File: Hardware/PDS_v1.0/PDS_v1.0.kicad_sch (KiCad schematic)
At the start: 28 parts, among them J1 Conn_01x02, J10 Conn_01x02, J11 Conn_01x02, J12 Conn_01x02, J13 Conn_01x04, J14 Conn_01x04, J15 Conn_01x03, J2 Conn_01x02, J3 Conn_01x02, J4 Conn_01x02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

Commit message: PDS done
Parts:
- added H1, H2, H3, H4: MountingHole, MountingHole:MountingHole_3.2mm_M3, symbol Mechanical:MountingHole
- added J6: Conn_01x02, Connector_Molex:Molex_KK-254_AE-6410-02A_1x02_P2.54mm_Vertical, symbol Connector_Generic:Conn_01x02
- J10: renamed from J8; footprint Connector_Molex:Molex_KK-254_AE-6410-03A_1x03_P2.54mm_Vertical -> Connector_Molex:Molex_KK-254_AE-6410-02A_1x02_P2.54mm_Vertical
- J11: renamed from J5; footprint Connector_Molex:Molex_KK-254_AE-6410-03A_1x03_P2.54mm_Vertical -> Connector_Molex:Molex_KK-254_AE-6410-02A_1x02_P2.54mm_Vertical
- J12: renamed from J6; footprint Connector_Molex:Molex_KK-254_AE-6410-03A_1x03_P2.54mm_Vertical -> Connector_Molex:Molex_KK-254_AE-6410-02A_1x02_P2.54mm_Vertical
- J13: renamed from J7; footprint Connector_Molex:Molex_KK-254_AE-6410-03A_1x03_P2.54mm_Vertical -> Connector_Molex:Molex_KK-254_AE-6410-02A_1x02_P2.54mm_Vertical
- J14: renamed from J10; footprint Connector_Molex:Molex_KK-254_AE-6410-03A_1x03_P2.54mm_Vertical -> Connector_Molex:Molex_KK-254_AE-6410-02A_1x02_P2.54mm_Vertical
- J15: renamed from J11; footprint Connector_Molex:Molex_KK-254_AE-6410-03A_1x03_P2.54mm_Vertical -> Connector_Molex:Molex_KK-254_AE-6410-02A_1x02_P2.54mm_Vertical
- J16: renamed from J12; footprint Connector_Molex:Molex_KK-254_AE-6410-03A_1x03_P2.54mm_Vertical -> Connector_Molex:Molex_KK-254_AE-6410-02A_1x02_P2.54mm_Vertical
- J3: renamed from J1; footprint Connector_Molex:Molex_KK-254_AE-6410-03A_1x03_P2.54mm_Vertical -> Connector_Molex:Molex_KK-254_AE-6410-02A_1x02_P2.54mm_Vertical
- J4: footprint Connector_Molex:Molex_KK-254_AE-6410-03A_1x03_P2.54mm_Vertical -> Connector_Molex:Molex_KK-254_AE-6410-02A_1x02_P2.54mm_Vertical
- J5: renamed from J9; footprint Connector_Molex:Molex_KK-254_AE-6410-03A_1x03_P2.54mm_Vertical -> Connector_Molex:Molex_KK-254_AE-6410-02A_1x02_P2.54mm_Vertical
- J8: renamed from J2; footprint Connector_Molex:Molex_KK-254_AE-6410-03A_1x03_P2.54mm_Vertical -> Connector_Molex:Molex_KK-254_AE-6410-02A_1x02_P2.54mm_Vertical
- J9: renamed from J3; footprint Connector_Molex:Molex_KK-254_AE-6410-03A_1x03_P2.54mm_Vertical -> Connector_Molex:Molex_KK-254_AE-6410-02A_1x02_P2.54mm_Vertical
- renumbered J13 to J1, J14 to J2, J15 to J7
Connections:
- net +5V: now also J11.2 (Pin_2), J12.2 (Pin_2), J13.2 (Pin_2), J4.1 (Pin_1), TP2.1
- net +3V3: now reaches J10.2 (Pin_2), J3.1 (Pin_1), J8.2 (Pin_2), J9.2 (Pin_2), TP1.1
- net +12V: now reaches J14.2 (Pin_2), J15.2 (Pin_2), J16.2 (Pin_2), J5.1 (Pin_1), TP3.1
- net at U1.10 (XIN): now also J6.1 (Pin_1)
- net at U1.11 (XOUT): now also J6.2 (Pin_2)
- no-connect marks 2 -> 0

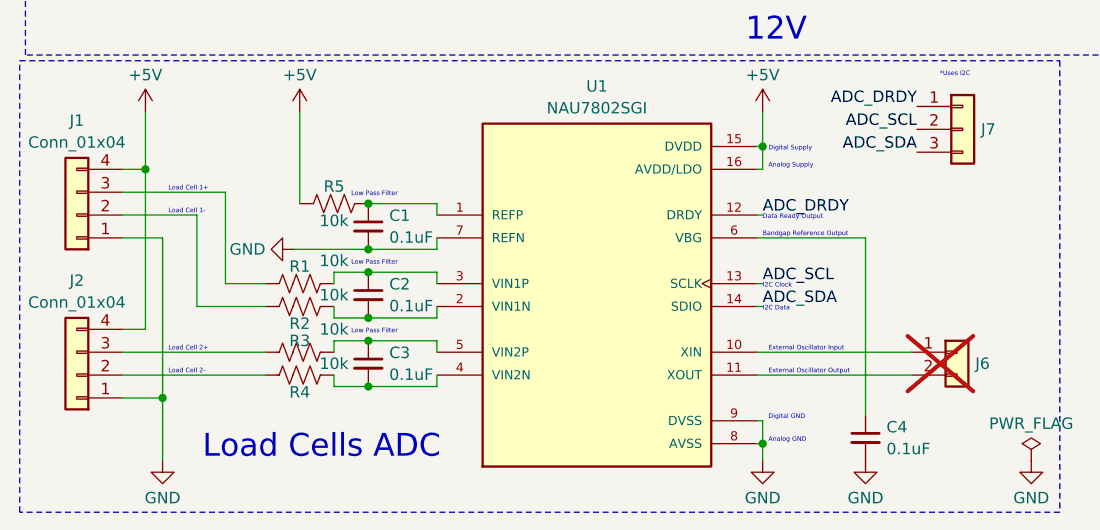
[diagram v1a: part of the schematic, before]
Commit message: fixed silkscreens + readability on PDS
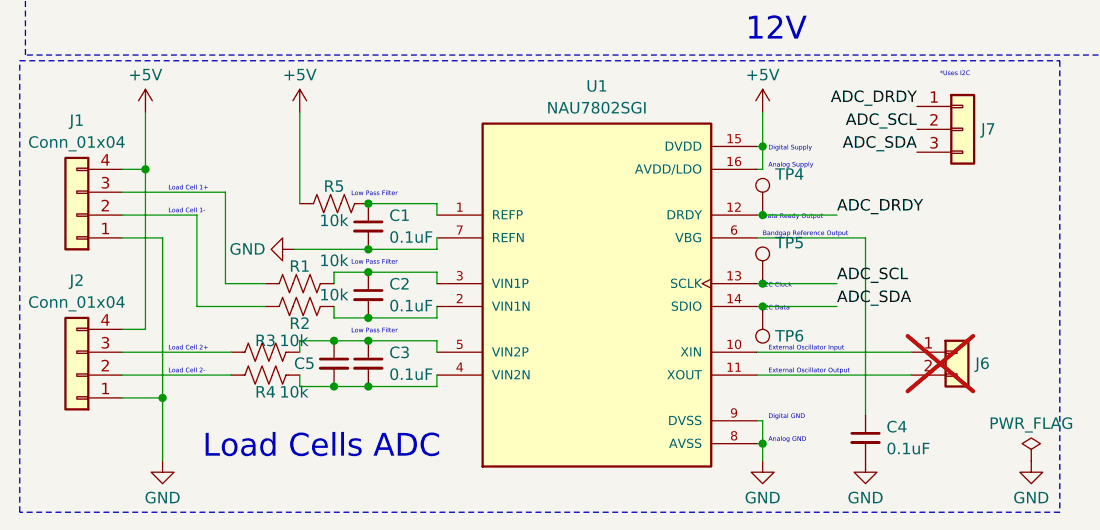
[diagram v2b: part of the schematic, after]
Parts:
- added C5: 470uF, Capacitor_THT:C_Radial_D10.0mm_H12.5mm_P5.00mm, symbol device:C_Small
- added TP4, TP5, TP6: TestPoint, TestPoint:TestPoint_Keystone_5010-5014_Multipurpose, symbol Connector:TestPoint
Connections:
- net ADC_DRDY: now also TP4.1
- net ADC_SCL: now also TP5.1
- net ADC_SDA: now also TP6.1
- net at C3.2, R4.2, U1.4 (VIN2N): now also C5.2
- net at C3.1, R3.2, U1.5 (VIN2P): now also C5.1
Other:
- moved on the sheet: R3, R4
